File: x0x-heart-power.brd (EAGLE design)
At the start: 100 x 80.8 mm, 13 parts, among them IC1 7805T, IC2 7812T, X0X-HEART POWER

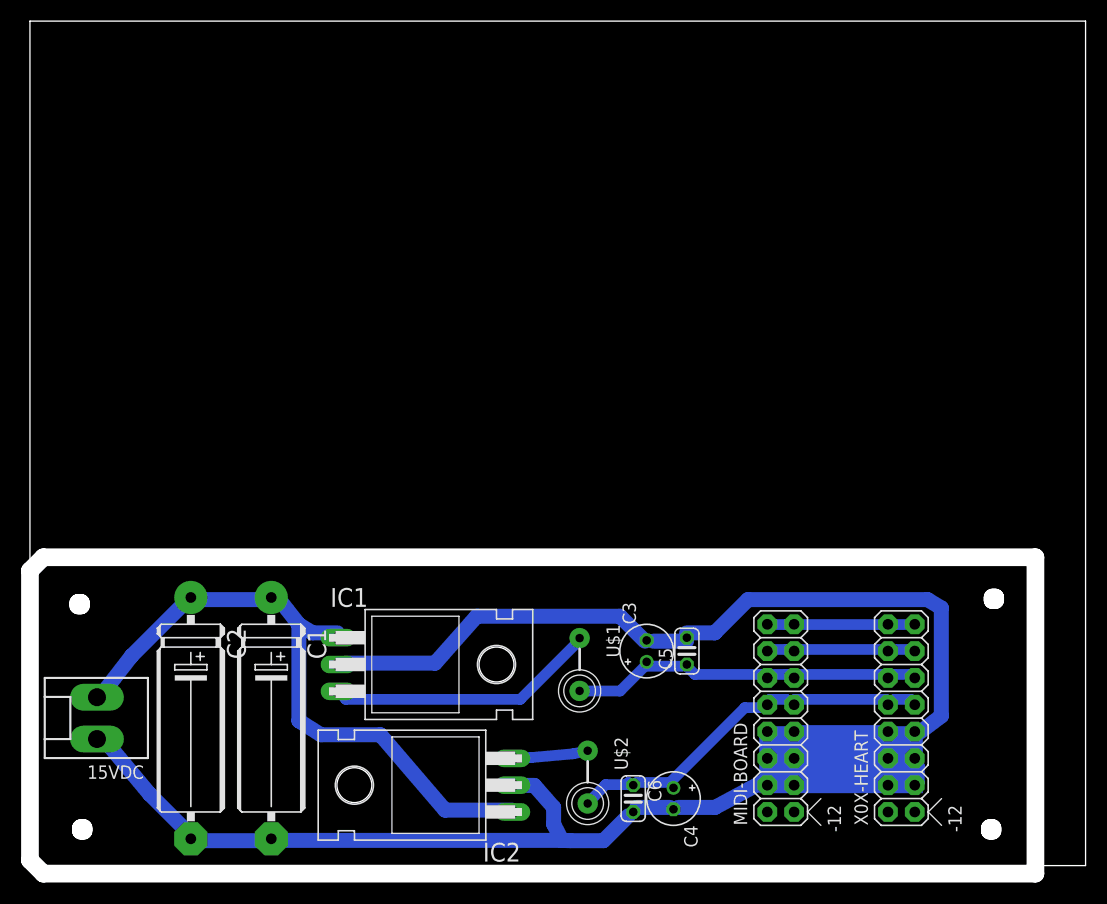
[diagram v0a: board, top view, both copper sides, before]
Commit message: added negative 12
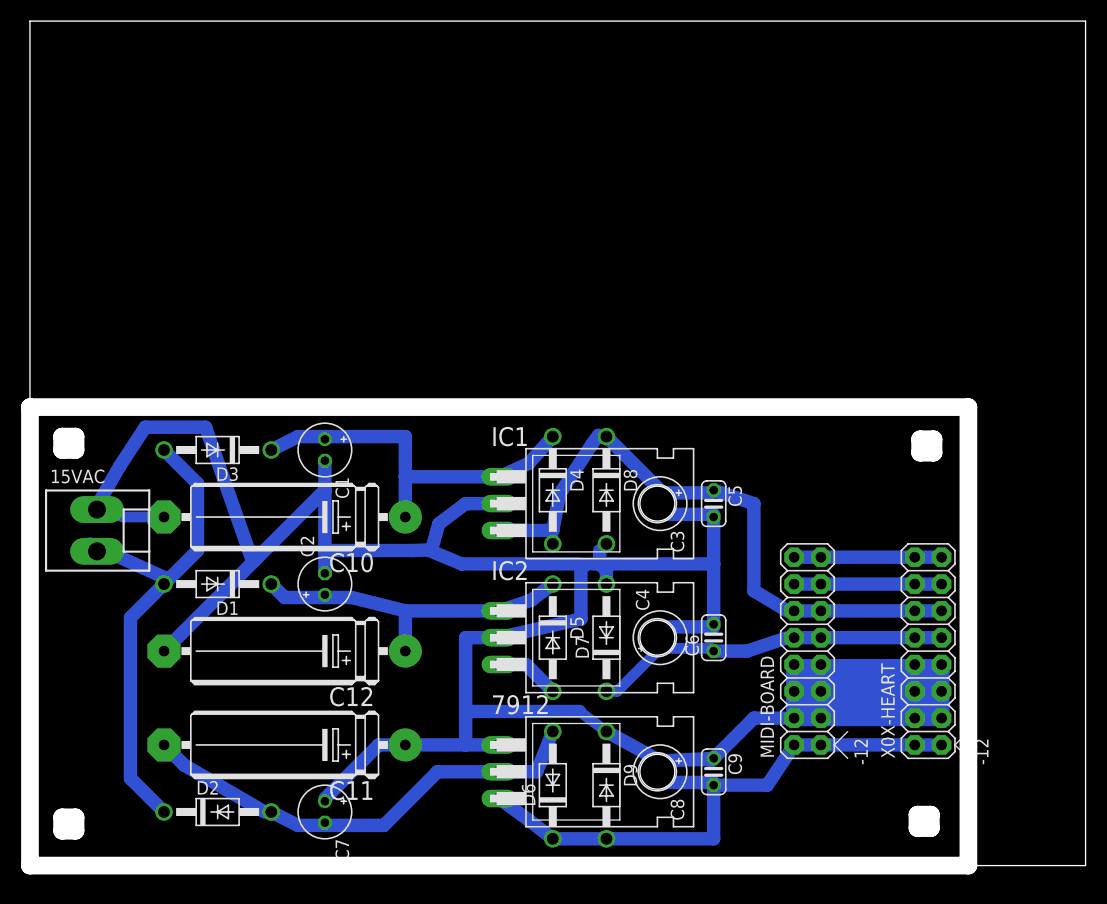
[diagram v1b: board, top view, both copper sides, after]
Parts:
- removed 15VDC: (no value), con-molex:KK-156-2
- removed U$1, U$2: FB, adafruit:FB
- added 15VAC: (no value), con-molex:KK-156-2
- added 7912: (no value), linear:TO220H
- added C10, C11, C12: 2200uF, rcl:E22-6
- added C7: 1uF, rcl:E2-5
- added C8: 10uF, rcl:E2-5
- added C9: 100n, rcl:C025-024X044
- added D1, D2, D3, D4, D5, D6, D7, D8, D9: 1N4004, diode:DO41-10
- C1, C2: value 200uF -> 1uF; device rcl:E22-6 -> rcl:E2-5
- moved C1 25.9 mm to (27.9, 39.4)
- moved IC2 23.6 mm to (54.6, 21.6), turned to 270 degrees
- moved IC1 21.6 mm to (54.6, 34.3)
- moved C2 18.0 mm to (27.9, 26.7), turned to 90 degrees
- moved C6 17.0 mm to (64.8, 21.6), turned to 90 degrees
- moved C4 15.3 mm to (59.7, 21.6), turned to 90 degrees
- moved C5 14.2 mm to (64.8, 34.3), turned to 270 degrees
- moved C3 14.0 mm to (59.7, 34.3), turned to 270 degrees
- moved X0X-HEART 6.84 mm to (85.1, 17.8)
- moved MIDI-BOARD 6.84 mm to (73.7, 17.8)
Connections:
- new net N$8: C12.+, C2.+, D1.C, D5.C, IC2.1
- new net N$9: 15VAC.2, D1.A, D2.C, D3.A
- net GND: now also 15VAC.1, 7912.1, C10.-, C11.+, C12.-, C7.+, C8.+, C9.1, D7.A, D8.A, D9.C; no longer 15VDC.1
- net N$3: now also D4.A, D8.C, IC1.3; no longer U$1.P$2
- net N$4: now also 7912.2, C11.-, C7.-, D2.A, D6.A; no longer IC1.3, U$1.P$1
- net N$5: now also 7912.3, C8.-, C9.2, D6.C, D9.A, MIDI-BOARD.1, MIDI-BOARD.2, X0X-HEART.1, X0X-HEART.2; no longer C4.+, C6.1, MIDI-BOARD.10, MIDI-BOARD.9, U$2.P$2, X0X-HEART.10, X0X-HEART.9
- net N$6: now also C10.+, D3.C, D4.C; no longer 15VDC.2, C2.+, IC2.1
- net N$7: now also C4.+, C6.1, D5.A, D7.C, MIDI-BOARD.10, MIDI-BOARD.9, X0X-HEART.10, X0X-HEART.9; no longer U$2.P$1
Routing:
- net GND: track 189.3 -> 263.3 mm
- net N$9: track 0.00 -> 50.5 mm
- net N$7: track 7.16 -> 39.9 mm
- net N$8: track 0.00 -> 32.1 mm
- net N$3: track 34.7 -> 60.6 mm
- net N$6: track 62.1 -> 36.3 mm
- net N$4: track 25.7 -> 44.1 mm
- net N$5: track 37.8 -> 55.6 mm
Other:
- board size 100 x 80.8 mm -> 100 x 80 mm

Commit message: tweaks
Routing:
- net N$5: track 55.6 -> 48.3 mm
- net GND: track 263.3 -> 265.9 mm
- net N$6: track 36.3 -> 34.0 mm
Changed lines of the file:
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@@
 <wire x1="35.56" y1="11.43" x2="33.02" y2="11.43" width="1.27" layer="16"/>
 <wire x1="27.94" y1="6.35" x2="27.94" y2="6.096" width="1.016" layer="16"/>
-<wire x1="35.56" y1="11.43" x2="41.275" y2="11.43" width="1.27" layer="16"/>
-<wire x1="41.275" y1="11.43" x2="44.45" y2="11.43" width="1.27" layer="16"/>
-<wire x1="41.275" y1="21.59" x2="44.45" y2="21.59" width="1.27" layer="16"/>
-<wire x1="41.275" y1="11.43" x2="41.275" y2="14.605" width="1.27" layer="16"/>
-<wire x1="41.275" y1="14.605" x2="41.275" y2="21.59" width="1.27" layer="16"/>
-<wire x1="41.275" y1="14.605" x2="52.07" y2="14.605" width="1.27" layer="16"/>
+<wire x1="35.56" y1="11.43" x2="40.005" y2="11.43" width="1.27" layer="16"/>
+<wire x1="40.005" y1="11.43" x2="44.45" y2="11.43" width="1.27" layer="16"/>
+<wire x1="40.005" y1="21.59" x2="44.45" y2="21.59" width="1.27" layer="16"/>
+<wire x1="40.005" y1="11.43" x2="40.005" y2="14.605" width="1.27" layer="16"/>
+<wire x1="40.005" y1="14.605" x2="40.005" y2="21.59" width="1.27" layer="16"/>
+<wire x1="40.005" y1="14.605" x2="52.07" y2="14.605" width="1.27" layer="16"/>
 <wire x1="64.77" y1="33.02" x2="64.77" y2="28.575" width="1.27" layer="16"/>
 <wire x1="64.77" y1="28.575" x2="64.77" y2="22.86" width="1.27" layer="16"/>
@@
 <wire x1="25.4" y1="40.64" x2="27.94" y2="40.64" width="1.27" layer="16"/>
 <wire x1="22.86" y1="39.37" x2="25.4" y2="40.64" width="1.27" layer="16"/>
-<wire x1="35.56" y1="40.64" x2="27.94" y2="40.64" width="1.27" layer="16"/>
+<wire x1="31.75" y1="40.64" x2="27.94" y2="40.64" width="1.27" layer="16"/>
 <wire x1="35.56" y1="33.02" x2="35.56" y2="36.83" width="1.27" layer="16"/>
-<wire x1="35.56" y1="36.83" x2="35.56" y2="40.64" width="1.27" layer="16"/>
+<wire x1="35.56" y1="36.83" x2="31.75" y2="40.64" width="1.27" layer="16"/>
 <wire x1="27.94" y1="40.64" x2="27.94" y2="40.386" width="1.016" layer="16"/>
 <wire x1="35.56" y1="36.83" x2="44.45" y2="36.83" width="1.27" layer="16"/>
@@
 <wire x1="72.39" y1="11.43" x2="74.93" y2="11.43" width="1.27" layer="16"/>
 <wire x1="74.93" y1="11.43" x2="83.82" y2="11.43" width="1.27" layer="16"/>
-<wire x1="64.77" y1="2.54" x2="54.61" y2="2.54" width="1.27" layer="16"/>
-<wire x1="64.77" y1="7.62" x2="64.77" y2="2.54" width="1.27" layer="16"/>
+<wire x1="55.88" y1="2.54" x2="54.61" y2="2.54" width="1.27" layer="16"/>
 <wire x1="59.69" y1="7.874" x2="64.77" y2="7.874" width="1.27" layer="16"/>
 <wire x1="64.77" y1="7.874" x2="64.77" y2="7.62" width="1.016" layer="16"/>
+<wire x1="55.88" y1="2.54" x2="58.42" y2="6.604" width="1.27" layer="16"/>
+<wire x1="58.42" y1="6.604" x2="59.69" y2="7.874" width="1.27" layer="16"/>
 </signal>
 <signal name="N$8">
